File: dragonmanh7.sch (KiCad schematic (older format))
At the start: 103 parts, among them J1 10118194-0001LF, J10 Conn_02x12_Odd_Even, J11 Conn_02x02_Odd_Even, J12 VBAT+, J13 PROTO1, J14 VBATG, J18 PROTO1, J2 10118194-0001LF, J3 RJ45_Amphenol_RJMG1BD3B8K1ANR, J4 Micro_SD_Card, J5 Screw_Terminal_01x06, J6 Conn_02x12_Odd_Even, J7 10118194-0001LF, J8 Screw_Terminal_01x02, J9 Conn_02x12_Odd_Even, SW1 RESET, SW2 PC13, U1 STM32H743VITx, U10 USBLC6-2SC6, U11 SN6505, U12 TCAN332, U13 ISL83483, U2 KSZ8081RNA, U3 ISO1050DUB, U4 ISO3082DW, U5 S25FL127SABMFI101, U6 AP63203, U7 USBLC6-2SC6, U8 STM32F042F6Px, U9 USBLC6-2SC6, Y1 8MHz, Y2 32.768KHz, Y3 25MHz

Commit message: Rename stupid name of trololo to more super-cool name dragonmanh7
Signed-off-by: Martin Ribelotta <martinribelotta@gmail.com>
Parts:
- J4: symbol trololo-rescue:Micro_SD_Card-Connector-trololo-rescue -> dragonmanh7-rescue:Micro_SD_Card-Connector-dragonmanh7-rescue-dragonmanh7-rescue
- U11: symbol trololo-rescue:SN6505-SN6505 -> dragonmanh7-rescue:SN6505-SN6505-dragonmanh7-rescue
- U3: symbol trololo-rescue:ISO1050DUB-Interface_CAN_LIN-trololo-rescue -> dragonmanh7-rescue:ISO1050DUB-Interface_CAN_LIN-dragonmanh7-rescue-dragonmanh7-rescue
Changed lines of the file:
@@
 EESchema Schematic File Version 4
-LIBS:trololo-cache
+LIBS:dragonmanh7-cache
 EELAYER 29 0
 EELAYER END
@@
 NoConn ~ 5550 9700
 $Comp
-L trololo-rescue:Micro_SD_Card-Connector-trololo-rescue J4
+L dragonmanh7-rescue:Micro_SD_Card-Connector-dragonmanh7-rescue-dragonmanh7-rescue J4
 U 1 1 5C625641
 P 7050 1250
@@
 	14950 5400 14950 5350
 $Comp
-L trololo-rescue:ISO1050DUB-Interface_CAN_LIN-trololo-rescue U3
+L dragonmanh7-rescue:ISO1050DUB-Interface_CAN_LIN-dragonmanh7-rescue-dragonmanh7-rescue U3
 U 1 1 5C76F366
 P 13550 3900
@@
 	12350 8350 12450 8350
 $Comp
-L trololo-rescue:SN6505-SN6505 U11
+L dragonmanh7-rescue:SN6505-SN6505-dragonmanh7-rescue U11
 U 1 1 5CA512D2
 P 13400 6750

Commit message: Change power and rs485/can connectors
Signed-off-by: Martin Ribelotta <martinribelotta@gmail.com>
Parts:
- J5: footprint Connector_Phoenix_MC:PhoenixContact_MC_1,5_6-GF-3.5_1x06_P3.50mm_Horizontal_ThreadedFlange_MountHole -> Connectors_Phoenix:PhoenixContact_MC-G_06x5.08mm_Angled
- J8: footprint Connector_Phoenix_MC:PhoenixContact_MC_1,5_2-GF-3.5_1x02_P3.50mm_Horizontal_ThreadedFlange_MountHole -> Connectors_Phoenix:PhoenixContact_MC-G_02x5.08mm_Angled
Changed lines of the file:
@@
 F 0 "J8" H 12150 9650 50  0000 L CNN
 F 1 "Screw_Terminal_01x02" H 11400 9350 50  0000 L CNN
-F 2 "Connector_Phoenix_MC:PhoenixContact_MC_1,5_2-GF-3.5_1x02_P3.50mm_Horizontal_ThreadedFlange_MountHole" H 12200 9550 50  0001 C CNN
+F 2 "Connectors_Phoenix:PhoenixContact_MC-G_02x5.08mm_Angled" H 12200 9550 50  0001 C CNN
 F 3 "~" H 12200 9550 50  0001 C CNN
 F 4 "1985195" H 400 100 50  0001 C CNN "manf#"
@@
 	1    8850 10200
 	0    -1   -1   0
-$EndComp
-$Comp
-L Connector:Screw_Terminal_01x06 J5
-U 1 1 5C7DFF3A
-P 15450 4450
-F 0 "J5" H 15450 4750 50  0000 C CNN
-F 1 "Screw_Terminal_01x06" V 15550 4450 50  0000 C CNN
-F 2 "Connector_Phoenix_MC:PhoenixContact_MC_1,5_6-GF-3.5_1x06_P3.50mm_Horizontal_ThreadedFlange_MountHole" H 15450 4450 50  0001 C CNN
-F 3 "~" H 15450 4450 50  0001 C CNN
-F 4 "1985234" H 0   0   50  0001 C CNN "manf#"
-	1    15450 4450
-	1    0    0    -1
 $EndComp
 Text Label 15250 4750 2    50   ~ 0
@@
 Wire Wire Line
 	13550 1700 13550 2450
+$Comp
+L Connector:Screw_Terminal_01x06 J5
+U 1 1 5C7DFF3A
+P 15450 4450
+F 0 "J5" H 15450 4750 50  0000 C CNN
+F 1 "Screw_Terminal_01x06" V 15550 4450 50  0000 C CNN
+F 2 "Connectors_Phoenix:PhoenixContact_MC-G_06x5.08mm_Angled" H 15450 4450 50  0001 C CNN
+F 3 "~" H 15450 4450 50  0001 C CNN
+F 4 "1985234" H 0   0   50  0001 C CNN "manf#"
+	1    15450 4450
+	1    0    0    -1
+$EndComp
 $EndSCHEMATC

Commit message: Update images and README
Signed-off-by: Martin Ribelotta <martinribelotta@gmail.com>
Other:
- note added: "COMM-CONN"
- note added: "COMM-ISO"
- note added: "COMM-ISO-PWR"
- note removed: "COMM"
- note removed: "COMM-PWR"
- moved on the sheet: C23, C24, C36, C37, C38, C39, C40, D1, D10, D11, D12, J5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

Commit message: Minimal changes for production based on prototipe pitfalls
 - Change bootloader jumper polarity
 - More spaces in some capacitores
 - Add SWD-M7 connector in path to debugger mcu

Signed-off-by: Martin Ribelotta <martinribelotta@gmail.com>
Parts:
- added J15: Conn_02x02_Odd_Even, Pin_Headers:Pin_Header_Straight_2x02_Pitch2.54mm, symbol Connector_Generic:Conn_02x02_Odd_Even
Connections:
- net +3V3: now also JP1.1; no longer R2.1
- net GND: now also R2.1, J15.2 (Pin_2); no longer JP1.1
- net SWCLK: now also J15.3 (Pin_3)
- net SWDIO: now also J15.1 (Pin_1)
- net ~RESET: now also J15.4 (Pin_4)
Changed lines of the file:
@@
 	1    0    0    -1
 $EndComp
-Wire Wire Line
-	1300 1750 1500 1750
-Connection ~ 1500 1750
 $Comp
 L power:GND #PWR0110
 U 1 1 5C59C578
-P 900 1750
-F 0 "#PWR0110" H 900 1500 50  0001 C CNN
-F 1 "GND" H 950 1600 50  0000 R CNN
-F 2 "" H 900 1750 50  0001 C CNN
-F 3 "" H 900 1750 50  0001 C CNN
-	1    900  1750
-	1    0    0    -1
+P 900 1550
+F 0 "#PWR0110" H 900 1300 50  0001 C CNN
+F 1 "GND" V 905 1422 50  0000 R CNN
+F 2 "" H 900 1550 50  0001 C CNN
+F 3 "" H 900 1550 50  0001 C CNN
+	1    900  1550
+	0    1    1    0
 $EndComp
-Wire Wire Line
-	900  1750 1100 1750
 $Comp
 L Device:Crystal_Small Y1
@@
 ENET_REF_CLK
 Wire Wire Line
-	900  1550 900  1750
-Connection ~ 900  1750
-Wire Wire Line
 	1100 2900 1100 3000
 Connection ~ 1100 3000
@@
 	1    0    0    -1
 $EndComp
-Wire Wire Line
-	1200 1300 1200 1250
-Wire Wire Line
-	1200 1250 1500 1250
-Wire Wire Line
-	1500 1250 1500 1300
 Text Label 9250 1900 0    50   ~ 0
 PA8
@@
 $EndComp
 Wire Wire Line
-	1500 1250 1500 1200
-Wire Wire Line
-	1500 1200 2600 1200
-Wire Wire Line
 	2600 1200 2600 1250
-Connection ~ 1500 1250
 Connection ~ 2600 1250
 Wire Wire Line
@@
 	1100 4300 1100 4500
 $Comp
-L power:+3.3V #PWR0184
-U 1 1 5CEBF9AC
-P 1100 3900
-F 0 "#PWR0184" H 1100 3750 50  0001 C CNN
-F 1 "+3.3V" V 1115 4028 50  0000 L CNN
-F 2 "" H 1100 3900 50  0001 C CNN
-F 3 "" H 1100 3900 50  0001 C CNN
-	1    1100 3900
-	1    0    0    -1
-$EndComp
-$Comp
 L Jumper:Jumper_2_Bridged JP5
 U 1 1 5CE929CB
@@
 Wire Notes Line
 	14200 5500 15750 5500
+$Comp
+L power:+3.3V #PWR0184
+U 1 1 5CEBF9AC
+P 1100 3900
+F 0 "#PWR0184" H 1100 3750 50  0001 C CNN
+F 1 "+3.3V" V 1115 4028 50  0000 L CNN
+F 2 "" H 1100 3900 50  0001 C CNN
+F 3 "" H 1100 3900 50  0001 C CNN
+	1    1100 3900
+	1    0    0    -1
+$EndComp
+$Comp
+L power:+3.3V #PWR05
+U 1 1 5CF89581
+P 1100 1750
+F 0 "#PWR05" H 1100 1600 50  0001 C CNN
+F 1 "+3.3V" V 1115 1878 50  0000 L CNN
+F 2 "" H 1100 1750 50  0001 C CNN
+F 3 "" H 1100 1750 50  0001 C CNN
+	1    1100 1750
+	0    -1   -1   0
+$EndComp
+Wire Wire Line
+	1200 1200 1200 1300
+Wire Wire Line
+	1200 1200 2600 1200
+Wire Wire Line
+	1300 1750 1500 1750
+Connection ~ 1500 1750
+$Comp
+L power:GND #PWR06
+U 1 1 5CFB2E42
+P 1500 1100
+F 0 "#PWR06" H 1500 850 50  0001 C CNN
+F 1 "GND" V 1505 972 50  0000 R CNN
+F 2 "" H 1500 1100 50  0001 C CNN
+F 3 "" H 1500 1100 50  0001 C CNN
+	1    1500 1100
+	0    1    1    0
+$EndComp
+Wire Wire Line
+	1500 1100 1500 1300
+$Comp
+L Connector_Generic:Conn_02x02_Odd_Even J15
+U 1 1 5CF91B73
+P 15200 950
+F 0 "J15" H 15250 1050 50  0000 C CNN
+F 1 "Conn_02x02_Odd_Even" H 15150 750 50  0000 C CNN
+F 2 "Pin_Headers:Pin_Header_Straight_2x02_Pitch2.54mm" H 15200 950 50  0001 C CNN
+F 3 "~" H 15200 950 50  0001 C CNN
+	1    15200 950
+	-1   0    0    1
+$EndComp
+Text Label 15400 850  0    50   ~ 0
+SWCLK
+Text Label 15400 950  0    50   ~ 0
+SWDIO
+Text Label 14900 850  2    50   ~ 0
+~RESET
+$Comp
+L power:GND #PWR07
+U 1 1 5CF92AFB
+P 14900 950
+F 0 "#PWR07" H 14900 700 50  0001 C CNN
+F 1 "GND" V 14905 822 50  0000 R CNN
+F 2 "" H 14900 950 50  0001 C CNN
+F 3 "" H 14900 950 50  0001 C CNN
+	1    14900 950
+	0    1    -1   0
+$EndComp
+$Comp
+L Graphic:Logo_Open_Hardware_Small #LOGO1
+U 1 1 5CFBA196
+P 10600 850
+F 0 "#LOGO1" H 10600 1125 50  0001 C CNN
+F 1 "Logo_Open_Hardware_Small" H 10600 625 50  0001 C CNN
+F 2 "footprints:ciaa_7-logo" H 10600 850 50  0001 C CNN
+F 3 "~" H 10600 850 50  0001 C CNN
+	1    10600 850
+	1    0    0    -1
+$EndComp
+$Comp
+L Graphic:Logo_Open_Hardware_Small #LOGO2
+U 1 1 5CFBA47B
+P 11300 850
+F 0 "#LOGO2" H 11300 1125 50  0001 C CNN
+F 1 "Logo_Open_Hardware_Small" H 11300 625 50  0001 C CNN
+F 2 "footprints:unqui-logo" H 11300 850 50  0001 C CNN
+F 3 "~" H 11300 850 50  0001 C CNN
+	1    11300 850
+	1    0    0    -1
+$EndComp
 $EndSCHEMATC

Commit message: Improve isolated area
Signed-off-by: Martin Ribelotta <martinribelotta@gmail.com>
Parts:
- removed J11: Conn_02x02_Odd_Even, Connector_PinHeader_2.54mm:PinHeader_2x02_P2.54mm_Vertical, symbol Connector_Generic:Conn_02x02_Odd_Even
- removed JP4: Jumper_2_Bridged, Jumper:SolderJumper-2_P1.3mm_Open_RoundedPad1.0x1.5mm, symbol Jumper:Jumper_2_Bridged
- added J11: Conn_02x03_Odd_Even, Connector_PinHeader_2.54mm:PinHeader_2x03_P2.54mm_Vertical, symbol Connector_Generic:Conn_02x03_Odd_Even
- added LOGO1: Logo_Open_Hardware_Small, footprints:ciaa_7-logo, symbol Graphic:Logo_Open_Hardware_Small
- added LOGO2: Logo_Open_Hardware_Small, footprints:unqui-logo, symbol Graphic:Logo_Open_Hardware_Small
- added R12, R13: 0R, Resistor_THT:R_Axial_DIN0204_L3.6mm_D1.6mm_P5.08mm_Horizontal, symbol Device:R_Small
- C17, C30, C31: manf# CL31B225KOHNNNE -> CL21B225KPFNNNE
- J4: symbol dragonmanh7-rescue:Micro_SD_Card-Connector-dragonmanh7-rescue-dragonmanh7-rescue -> dragonmanh7-rescue:Micro_SD_Card-Connector-dragonmanh7-rescue-dragonmanh7-rescue-dragonmanh7-rescue
- JP1: footprint Connector_PinHeader_2.54mm:PinHeader_1x02_P2.54mm_Horizontal -> Connector_PinHeader_2.54mm:PinHeader_1x02_P2.54mm_Vertical
- U11: symbol dragonmanh7-rescue:SN6505-SN6505-dragonmanh7-rescue -> dragonmanh7-rescue:SN6505-SN6505-dragonmanh7-rescue-dragonmanh7-rescue
- U3: symbol dragonmanh7-rescue:ISO1050DUB-Interface_CAN_LIN-dragonmanh7-rescue-dragonmanh7-rescue -> dragonmanh7-rescue:ISO1050DUB-Interface_CAN_LIN-dragonmanh7-rescue-dragonmanh7-rescue-dragonmanh7-rescue
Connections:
- net +3V3: now also J11.1 (Pin_1), R13.2; no longer R7.1, U13.8 (VCC)
- net +5P: now also U13.8 (VCC), R13.1
- net BOOT0_B: now also J11.2 (Pin_2)
- net GND: now also R7.1, J11.3 (Pin_3), R12.2; no longer U13.5 (GND)
- net GNDPWR: now also U13.5 (GND), R12.1
- net SWCLK_B: now also J11.6 (Pin_6)
- net SWDIO_B: now also J11.5 (Pin_5)
- net DBG_RST: now reaches C27.2, U8.4 (NRST)
- net DBG_RST: now also J11.4 (Pin_4)
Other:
- note added: "GND/VCC shunt:\nconnect this for use\nwith non-isolated\ncomponents"
- moved on the sheet: C1, C10, C11, C12, C13, C14, C15, C16, C17, C18, C19, C2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

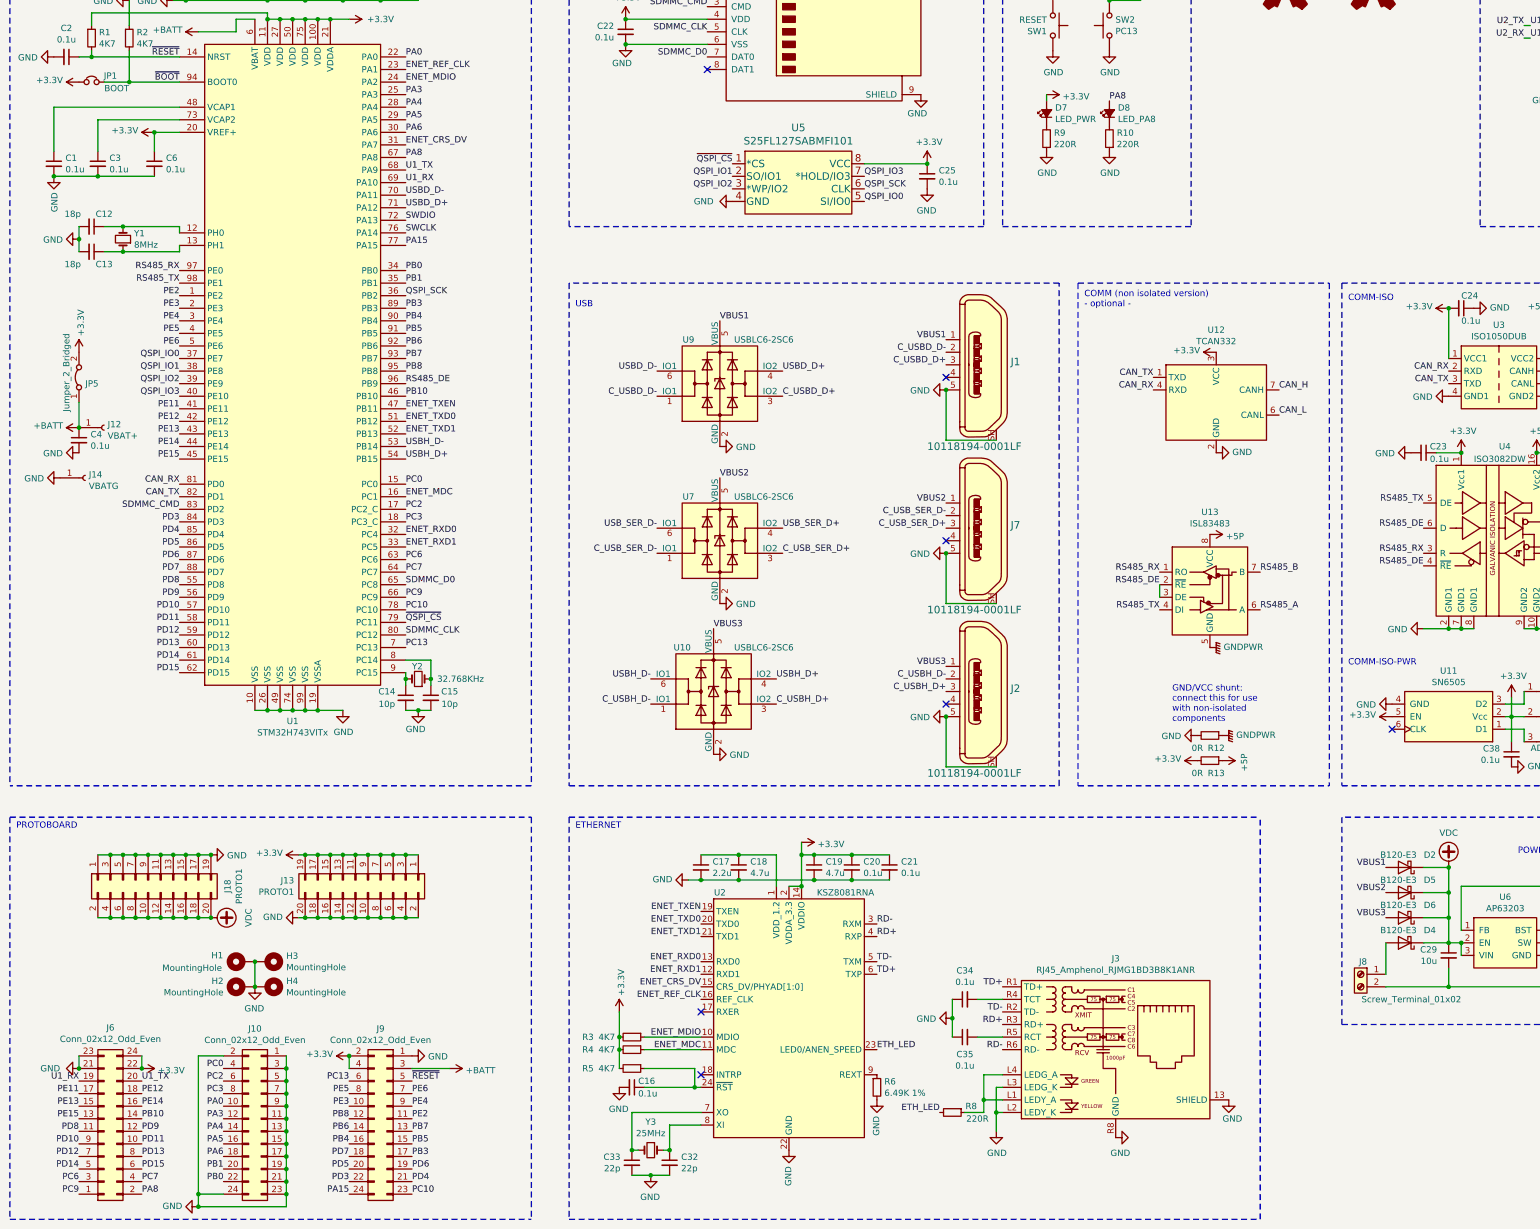
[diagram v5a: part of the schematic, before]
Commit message: Add usb host power controller
Signed-off-by: Martin Ribelotta <martinribelotta@gmail.com>
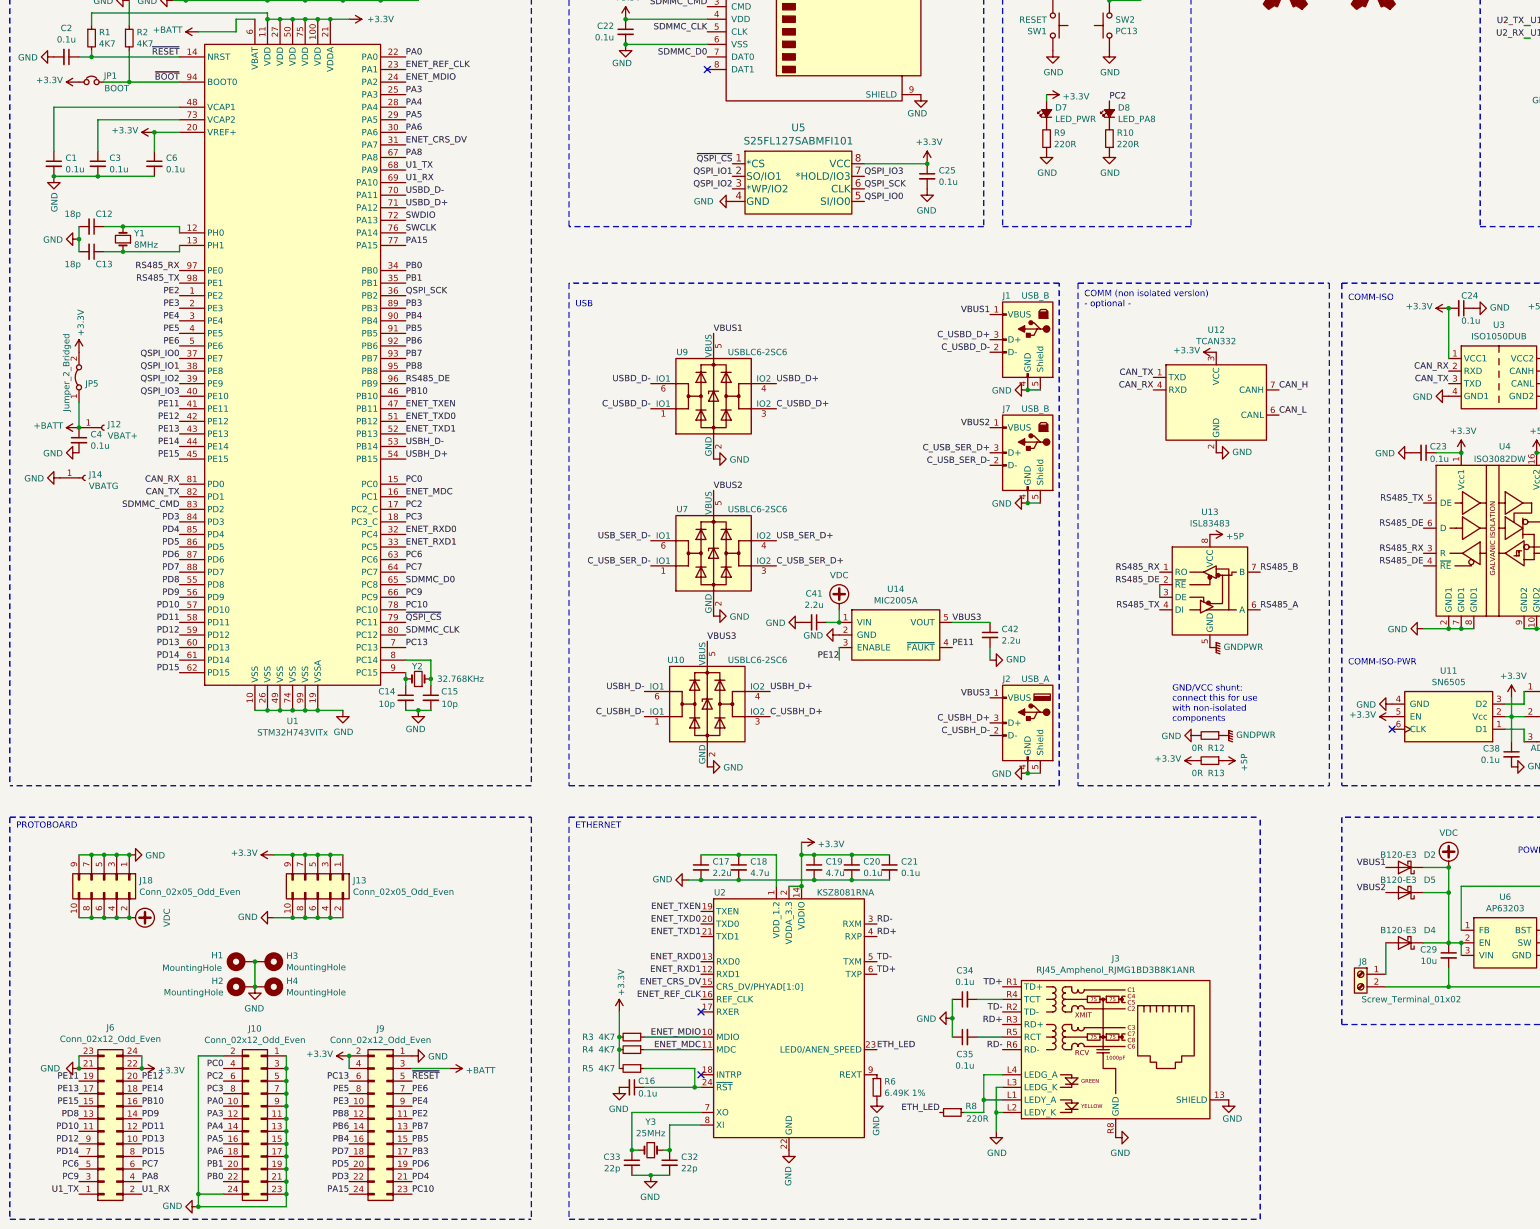
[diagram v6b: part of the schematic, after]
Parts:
- removed D6: B120-E3, Diode_SMD:D_SMA, symbol Diode:B120-E3
- removed J1, J2, J7: 10118194-0001LF, footprints:USB_Micro_B_Female_10118194-0001LF, symbol dk_USB-DVI-HDMI-Connectors:10118194-0001LF
- removed J13, J18: PROTO1, Connector_PinHeader_2.54mm:PinHeader_2x10_P2.54mm_Vertical, symbol Connector_Generic:Conn_02x10_Odd_Even
- added C41, C42: 2.2u, Capacitor_SMD:C_0805_2012Metric, symbol Device:C_Small
- added J1, J7: USB_B, Connector_USB:USB_B_OST_USB-B1HSxx_Horizontal, symbol Connector:USB_B
- added J13, J18: Conn_02x05_Odd_Even, Connector_PinSocket_2.54mm:PinSocket_2x05_P2.54mm_Vertical, symbol Connector_Generic:Conn_02x05_Odd_Even
- added J2: USB_A, footprints:USB_A_Female_Vertical_RA_73725-0110BLF, symbol Connector:USB_A
- added U14: MIC2005A, Package_TO_SOT_SMD:SOT-23-5, symbol mic20xx:MIC2005A
- D2, D4, D5: footprint Diode_SMD:D_SMA -> Diode_SMD:D_SOD-123
- JP1: footprint Connector_PinHeader_2.54mm:PinHeader_1x02_P2.54mm_Vertical -> Connector_PinHeader_2.54mm:PinHeader_1x02_P2.54mm_Horizontal
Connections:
- net +3V3: now also J13.1 (Pin_1), J13.3 (Pin_3), J13.5 (Pin_5), J13.7 (Pin_7), J13.9 (Pin_9)
- net C_USBD_D+: now also J1.3 (D+)
- net C_USBD_D-: now also J1.2 (D-)
- net C_USBH_D+: now also J2.3 (D+)
- net C_USBH_D-: now also J2.2 (D-)
- net C_USB_SER_D+: now also J7.3 (D+)
- net C_USB_SER_D-: now also J7.2 (D-)
- net GND: now also C41.2, C42.2, J1.4 (GND), J1.5 (Shield), J13.10 (Pin_10), J13.2 (Pin_2), J13.4 (Pin_4), J13.6 (Pin_6), J13.8 (Pin_8), J18.1 (Pin_1), J18.3 (Pin_3), J18.5 (Pin_5), J18.7 (Pin_7), J18.9 (Pin_9), J2.4 (GND), J2.5 (Shield), J7.4 (GND), J7.5 (Shield), U14.2 (GND)
- net PA8: now also J6.4 (Pin_4); no longer D8.2 (A), J6.2 (Pin_2)
- net PB10: now also J6.16 (Pin_16); no longer J6.14 (Pin_14)
- net PC2: now also D8.2 (A)
- net PC6: now also J6.5 (Pin_5); no longer J6.3 (Pin_3)
- net PC7: now also J6.6 (Pin_6); no longer J6.4 (Pin_4)
- net PC9: now also J6.3 (Pin_3); no longer J6.1 (Pin_1)
- net PD10: now also J6.11 (Pin_11); no longer J6.9 (Pin_9)
- net PD11: now also J6.12 (Pin_12); no longer J6.10 (Pin_10)
- net PD12: now also J6.9 (Pin_9); no longer J6.7 (Pin_7)
- net PD13: now also J6.10 (Pin_10); no longer J6.8 (Pin_8)
- net PD14: now also J6.7 (Pin_7); no longer J6.5 (Pin_5)
- net PD15: now also J6.8 (Pin_8); no longer J6.6 (Pin_6)
- net PD8: now also J6.13 (Pin_13); no longer J6.11 (Pin_11)
- net PD9: now also J6.14 (Pin_14); no longer J6.12 (Pin_12)
- net PE11: now also J6.19 (Pin_19), U14.4 (~FAUKT); no longer J6.17 (Pin_17)
- net PE12: now also J6.20 (Pin_20), U14.3 (ENABLE); no longer J6.18 (Pin_18)
- net PE13: now also J6.17 (Pin_17); no longer J6.15 (Pin_15)
- net PE14: now also J6.18 (Pin_18); no longer J6.16 (Pin_16)
- net PE15: now also J6.15 (Pin_15); no longer J6.13 (Pin_13)
- net U1_RX: now also J6.2 (Pin_2); no longer J6.19 (Pin_19)
- net U1_TX: now also J6.1 (Pin_1); no longer J6.20 (Pin_20)
- net VBUS1: now also J1.1 (VBUS)
- net VBUS2: now also J7.1 (VBUS)
- net VBUS3: now also C42.1, J2.1 (VBUS), U14.5 (VOUT)
- net VDC: now also C41.1, J18.10 (Pin_10), J18.2 (Pin_2), J18.4 (Pin_4), J18.6 (Pin_6), J18.8 (Pin_8), U14.1 (VIN)
- no-connect marks 15 -> 12
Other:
- moved on the sheet: U10, U7, U9
